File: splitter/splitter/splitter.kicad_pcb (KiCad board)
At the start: 2 copper layers, 52 x 92.4 mm, 41 parts, among them J1 JACKIN, J10 Conn_01x08, J11 Conn_01x08, J2 JACKSEND, J3 JACKRECV, J4 JACKOUT, J5 Jack-DC, J6 JACKSEND2, J8 JACKRECV2, SW1 SW_MODE, SW2 SW_BYPASS, U1 TL074, U2 TLE2426xLP

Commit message: updated generated outputs and docs
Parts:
- C1, C2: value 22n -> 6.8n
- C3, C4: value .1u -> 1u
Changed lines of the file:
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@@
       (effects (font (size 1 1) (thickness 0.15)))
     )
-    (fp_text value "22n" (at 2.5 0) (layer "F.SilkS")
+    (fp_text value "6.8n" (at 2.5 0) (layer "F.SilkS")
       (effects (font (size 1 1) (thickness 0.15)))
     )
@@
       (effects (font (size 1 1) (thickness 0.15)))
     )
-    (fp_text value "22n" (at 2.5 0) (layer "F.SilkS")
+    (fp_text value "6.8n" (at 2.5 0) (layer "F.SilkS")
       (effects (font (size 1 1) (thickness 0.15)))
     )
@@
       (effects (font (size 1 1) (thickness 0.15)))
     )
-    (fp_text user "${REFERENCE}" (at 3.81 7.62) (layer "F.Fab")
+    (fp_text user "${REFERENCE}" (at 3.81 7.62) (layer "F.Fab") hide
       (effects (font (size 1 1) (thickness 0.15)))
     )
@@
       (effects (font (size 1 1) (thickness 0.15)))
     )
-    (fp_text value ".1u" (at 1.25 3.75 90) (layer "F.Fab")
+    (fp_text value "1u" (at 1.25 3.75 90) (layer "F.Fab")
       (effects (font (size 1 1) (thickness 0.15)))
     )
@@
       (effects (font (size 1 1) (thickness 0.15)))
     )
-    (fp_text value ".1u" (at 1.25 3.75 90) (layer "F.Fab")
+    (fp_text value "1u" (at 1.25 3.75 90) (layer "F.Fab")
       (effects (font (size 1 1) (thickness 0.15)))
     )
@@
     (effects (font (size 1 1) (thickness 0.15)) (justify left))
   )
-  (gr_text "JLCJLCJLCJLC" (at 5.08 61.452 90) (layer "F.SilkS")
+  (gr_text "JLCJLCJLCJLC" (at 55 61.8 90) (layer "F.SilkS")
     (effects (font (size 1 1) (thickness 0.15)))
   )

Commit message: rev e
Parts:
- removed the R4 at (27.5, 60.5)
- removed the R5 at (32.0, 60.5)
- C2: renamed from C1; footprint kicad-official/Capacitor_THT.pretty:C_Disc_D4.3mm_W1.9mm_P5.00mm -> kicad-official/Capacitor_THT.pretty:C_Rect_L7.0mm_W2.5mm_P5.00mm
- C3: renamed from C2; footprint kicad-official/Capacitor_THT.pretty:C_Disc_D4.3mm_W1.9mm_P5.00mm -> kicad-official/Capacitor_THT.pretty:C_Rect_L7.0mm_W2.5mm_P5.00mm
- moved R6 8.81 mm to (50.5, 34.8), turned to 180 degrees
- moved R4 7.62 mm to (40.9, 45.2), turned to 90 degrees
- moved C1 6.68 mm to (27.2, 56.1), turned to 0 degrees
- moved C5 5.00 mm to (37.3, 43.6), turned to 90 degrees
- moved C8 4.54 mm to (32.2, 59.7), turned to 180 degrees
- moved C7 3.94 mm to (49.0, 30.8)
- moved C6 0.13 mm to (19.5, 37.4)
- renumbered C5 to C1, C4 to C10, C7 to C4, C6 to C5, C8 to C6, C9 to C7, C10 to C8, C3 to C9, J6 to J3, J3 to J4, J8 to J5, J4 to J6, J5 to J7, J10 to J8, J11 to J9, JP2 to JP1, JP1 to JP2, R9 to R10, R6 to R4, R7 to R5, R8 to R6, R10 to R7, R11 to R8, R12 to R9, SW2 to SW1, SW1 to SW2
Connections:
- C1 pad 1: Net-(C5-Pad1) -> Net-(C1-Pad1)
- C4 pad 1: /SEND_2 -> Net-(C4-Pad1)
- C4 pad 2: Net-(C7-Pad2) -> /HIGH
- C5 pad 1: Net-(C6-Pad1) -> Net-(C5-Pad1)
- C5 pad 2: /SEND_1 -> /LOW
- R3 pad 2: /HIGH -> Net-(C4-Pad1)
- R4 pad 1: /LOW -> Net-(C5-Pad1)
- RV1 pad 5: /HIGH -> Net-(C4-Pad1)
- RV1 pad 6: /HIGH -> Net-(C4-Pad1)
- SW2 pad 2: /HALF_IN -> /IN
- SW2 pad 3: Net-(C6-Pad1) -> /SEND_1
- SW2 pad 6: /HALF_IN -> /IN
- SW2 pad 7: Net-(C7-Pad2) -> /SEND_2
- U1 pad 1: /HIGH -> Net-(C4-Pad1)
- U1 pad 12: /HALF_IN -> Net-(C1-Pad1)
- U1 pad 14: /LOW -> Net-(C5-Pad1)
- U1 pad 2: /HIGH -> Net-(C4-Pad1)
- U1 pad 5: Net-(C5-Pad1) -> Net-(C1-Pad1)
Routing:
- net /HALF_IN: track 54.9 -> 0.00 mm
- net Net-(C4-Pad1): track 0.00 -> 51.1 mm, vias 0 -> 1
- net /IN: track 31.7 -> 71.0 mm, vias 0 -> 1
- net /SEND_1: track 30.7 -> 55.8 mm
- net /HIGH: track 44.5 -> 20.9 mm, vias 1 -> 0
- net Net-(C1-Pad1): track 0.00 -> 22.3 mm
- net Net-(C6-Pad1): track 22.2 -> 0.00 mm, vias 1 -> 0
- net GND: track 82.2 -> 63.9 mm
- net Net-(C7-Pad2): track 12.4 -> 0.00 mm
- net /SEND_2: track 82.8 -> 73.4 mm
- net Net-(C5-Pad1): track 22.3 -> 15.6 mm
- net Net-(C7-Pad1): track 4.52 -> 9.59 mm
- net /LOW: track 31.3 -> 27.4 mm
- net /RECV_2: track 94.8 -> 91.2 mm
- net Net-(C8-Pad1): track 29.5 -> 32.2 mm
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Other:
- board size 52 x 92.4 mm -> 52 x 92.5 mm
- board text added: "REV.E TONE SPLITTER 2023-09-28"
- board text removed: "REV.D TONE SPLITTER 2023-08-31"

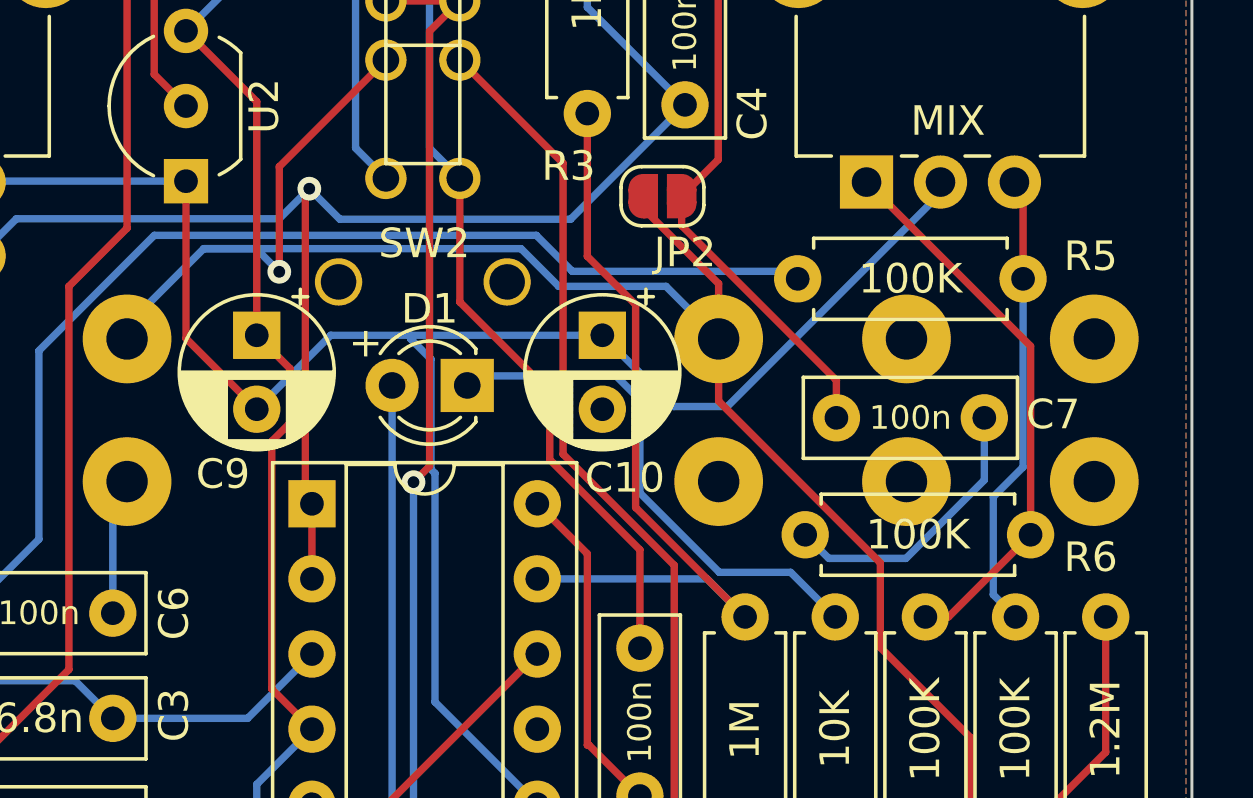
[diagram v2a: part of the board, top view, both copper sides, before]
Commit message: update capacitor footprints
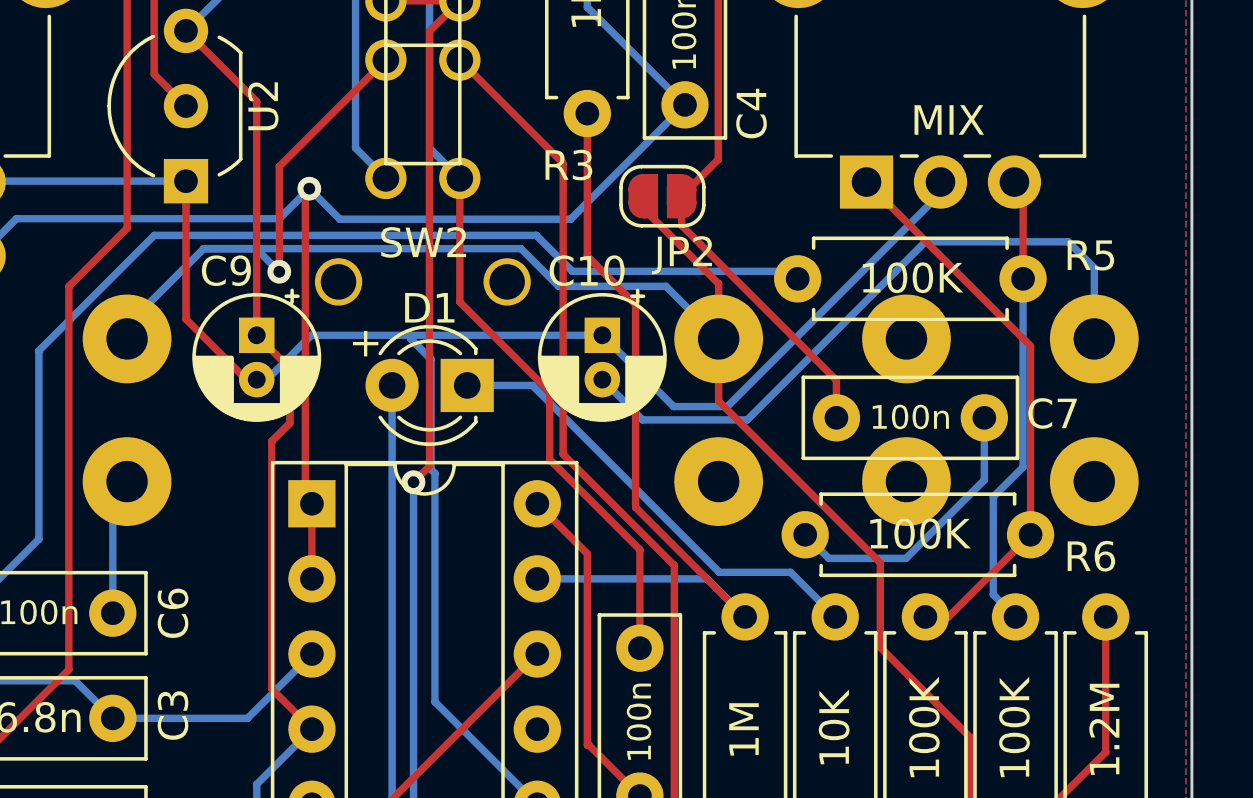
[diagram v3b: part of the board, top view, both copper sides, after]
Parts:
- C10, C9: footprint kicad-official/Capacitor_THT.pretty:CP_Radial_D5.0mm_P2.50mm -> kicad-official/Capacitor_THT.pretty:CP_Radial_D4.0mm_P1.50mm
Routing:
- net GNDD: track 10.1 -> 32.5 mm
- net GND: track 63.9 -> 62.0 mm
- net Net-(D1-Pad1): track 17.3 -> 15.7 mm

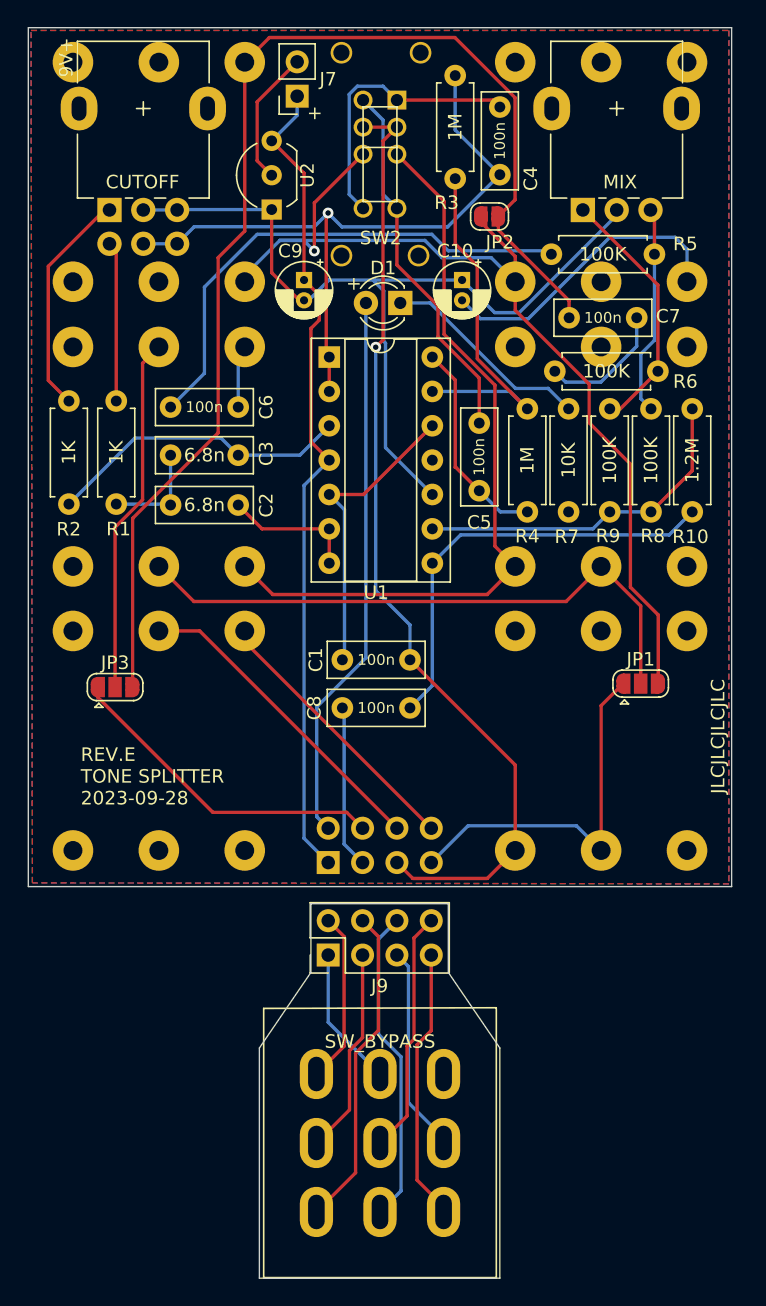
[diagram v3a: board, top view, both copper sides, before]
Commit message: switch to IPC cables for switch
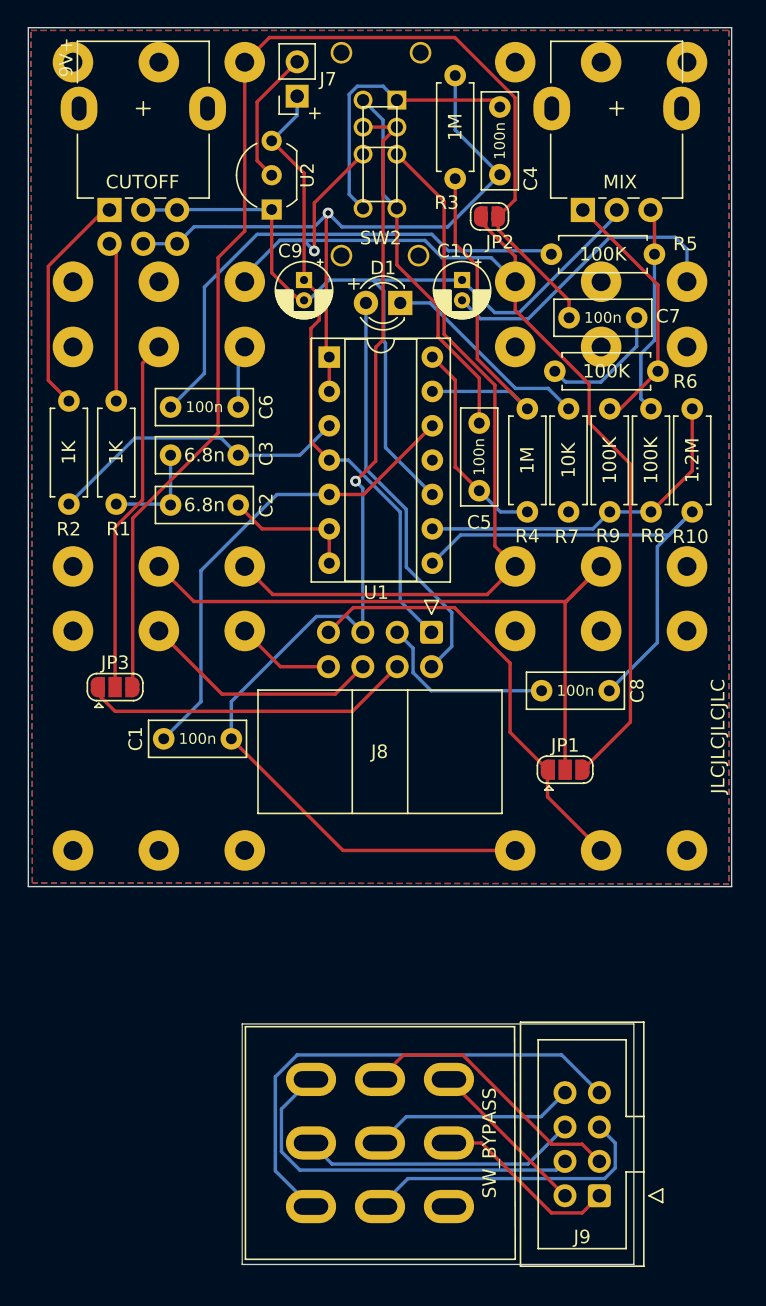
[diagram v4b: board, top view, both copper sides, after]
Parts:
- J8: footprint kicad-official/Connector_PinSocket_2.54mm.pretty:PinSocket_2x04_P2.54mm_Vertical -> kicad-official/Connector_IDC.pretty:IDC-Header_2x04_P2.54mm_Horizontal; moved to F.Cu
- J9: footprint kicad-official/Connector_PinHeader_2.54mm.pretty:PinHeader_2x04_P2.54mm_Vertical -> kicad-official/Connector_IDC.pretty:IDC-Header_2x04_P2.54mm_Vertical
- moved J9 26.8 mm to (46.2, 95.8), turned to 180 degrees
- moved J8 18.7 mm to (33.8, 54.1)
- moved C8 14.8 mm to (47.0, 58.4)
- moved C1 14.4 mm to (14.0, 62.0)
- moved JP1 8.47 mm to (43.7, 64.3)
- turned SW1 to -90 degrees
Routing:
- net /INR_B: track 19.3 -> 36.5 mm
- net +9V: track 61.2 -> 46.7 mm
- net Net-(C1-Pad1): track 22.3 -> 35.1 mm
- net /OUTT: track 19.5 -> 7.28 mm
- net /LED: track 40.7 -> 30.1 mm
- net /IN: track 71.0 -> 81.3 mm
- net /IN_B: track 14.2 -> 22.1 mm
- net /SEND_2: track 73.4 -> 80.4 mm
- net Net-(J2-PadR): track 44.7 -> 51.0 mm
- net /OUTR: track 23.6 -> 17.9 mm
- net /INR: track 27.4 -> 32.5 mm
- net /OUT_B: track 15.3 -> 20.3 mm
- net Net-(C8-Pad1): track 32.2 -> 36.6 mm
- net /RECVR_B: track 23.9 -> 28.0 mm
- net /9V_B: track 10.4 -> 13.8 mm
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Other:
- board size 52 x 92.5 mm -> 52 x 91.4 mm

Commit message: update input buffer
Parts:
- added R11: 1M, Resistor_THT:R_Axial_DIN0207_L6.3mm_D2.5mm_P7.62mm_Horizontal, F.Cu at (11.5, 58.0)
- added R12: 1M, Resistor_THT:R_Axial_DIN0207_L6.3mm_D2.5mm_P7.62mm_Horizontal, F.Cu at (7.00, 58.0)
- C1, C4, C5, C6, C7, C8: value 100n -> 10u; footprint kicad-official/Capacitor_THT.pretty:C_Rect_L7.0mm_W2.5mm_P5.00mm -> Capacitor_SMD:C_0805_2012Metric
- C10, C9: footprint kicad-official/Capacitor_THT.pretty:CP_Radial_D4.0mm_P1.50mm -> Capacitor_SMD:C_0805_2012Metric
- C2, C3: footprint kicad-official/Capacitor_THT.pretty:C_Rect_L7.0mm_W2.5mm_P5.00mm -> Capacitor_THT:C_Rect_L7.0mm_W2.5mm_P5.00mm
- D1: footprint kicad-official/LED_THT.pretty:LED_D3.0mm -> LED_THT:LED_D3.0mm
- J1, J2, J3, J4, J5, J6: footprint kicad-legacy/kicad-footprints/Connector_Audio.pretty:Jack_6.35mm_Neutrik_NMJ6HFD2_Horizontal -> Connector_Audio:Jack_6.35mm_Neutrik_NMJ6HFD2_Horizontal
- R1, R10, R2, R3, R4, R5, R6, R7, R8, R9: footprint kicad-official/Resistor_THT.pretty:R_Axial_DIN0207_L6.3mm_D2.5mm_P7.62mm_Horizontal -> Resistor_THT:R_Axial_DIN0207_L6.3mm_D2.5mm_P7.62mm_Horizontal
- RV1: value CUTOFF -> A1M_DUAL_CUTOFF; footprint kicad-official/Potentiometer_THT.pretty:Potentiometer_Alpha_RD902F-40-00D_Dual_Vertical -> Potentiometer_THT:Potentiometer_Alpha_RD902F-40-00D_Dual_Vertical
- RV2: value MIX -> B10K_MIX; footprint kicad-official/Potentiometer_THT.pretty:Potentiometer_Alpha_RD901F-40-00D_Single_Vertical -> Potentiometer_THT:Potentiometer_Alpha_RD901F-40-00D_Single_Vertical
- moved JP3 6.29 mm to (16.7, 58.0)
- moved C1 4.22 mm to (16.9, 65.0)
- moved C4 1.77 mm to (38.8, 18.5), turned to -90 degrees
- moved C6 1.55 mm to (21.0, 37.0), turned to -90 degrees
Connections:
- C2 pad 2: Net-(C2-Pad2) -> Net-(U1D-+)
- U1 pad 12: Net-(C1-Pad1) -> Net-(U1D-+)
- U1 pad 5: Net-(C1-Pad1) -> GND
- U1 pad 6: Net-(C2-Pad2) -> Net-(U1B--)
- U1 pad 7: Net-(C2-Pad2) -> Net-(U1D-+)
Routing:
- net Net-(U1D-+): track 0.00 -> 46.6 mm, vias 0 -> 1
- net Net-(U1B--): track 0.00 -> 36.5 mm, vias 0 -> 1
- net Net-(C1-Pad1): track 35.1 -> 4.76 mm
- net Net-(U1D--): track 26.8 -> 0.00 mm
- net Net-(C2-Pad2): track 10.0 -> 0.00 mm
- net +9V: track 46.7 -> 37.2 mm
- net /IN: track 81.3 -> 89.8 mm, vias 1 -> 2
- net /RECVR: track 24.6 -> 18.6 mm
- net /RECV_2: track 91.2 -> 96.4 mm
- net Net-(JP3-C): track 26.5 -> 30.2 mm
- net Net-(C6-Pad2): track 37.4 -> 39.8 mm, vias 0 -> 1
- net /HIGH: track 20.9 -> 22.5 mm
- net Net-(U1A--): track 51.1 -> 52.5 mm
- net GNDD: track 32.5 -> 33.6 mm
- net /OUTR: track 17.9 -> 17.1 mm
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
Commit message: redesign board: rev F
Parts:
- C2, C3: footprint Capacitor_THT:C_Rect_L7.0mm_W2.5mm_P5.00mm -> Capacitor_SMD:C_0805_2012Metric
- J7: footprint kicad-official/Connector_PinSocket_2.54mm.pretty:PinSocket_1x02_P2.54mm_Vertical -> Connector_PinSocket_2.54mm:PinSocket_1x02_P2.54mm_Vertical
- J8: footprint kicad-official/Connector_IDC.pretty:IDC-Header_2x04_P2.54mm_Horizontal -> Connector_IDC:IDC-Header_2x04_P2.54mm_Vertical
- J9: footprint kicad-official/Connector_IDC.pretty:IDC-Header_2x04_P2.54mm_Vertical -> Connector_IDC:IDC-Header_2x04_P2.54mm_Vertical
- JP1, JP3: footprint kicad-official/Jumper.pretty:SolderJumper-3_P1.3mm_Open_RoundedPad1.0x1.5mm -> Jumper:SolderJumper-3_P1.3mm_Open_RoundedPad1.0x1.5mm
- JP2: footprint kicad-official/Jumper.pretty:SolderJumper-2_P1.3mm_Open_RoundedPad1.0x1.5mm -> Jumper:SolderJumper-2_P1.3mm_Open_RoundedPad1.0x1.5mm
- R1, R10, R11, R12, R2, R3, R4, R5, R6, R8, R9: footprint Resistor_THT:R_Axial_DIN0207_L6.3mm_D2.5mm_P7.62mm_Horizontal -> Resistor_SMD:R_0805_2012Metric
- R7: value 10K -> 100K; footprint Resistor_THT:R_Axial_DIN0207_L6.3mm_D2.5mm_P7.62mm_Horizontal -> Resistor_SMD:R_0805_2012Metric
- U1: footprint kicad-official/Package_DIP.pretty:DIP-14_W7.62mm_Socket -> Package_DIP:DIP-14_W7.62mm_Socket
- U2: footprint kicad-official/Package_TO_SOT_THT.pretty:TO-92_Inline_Wide -> Package_TO_SOT_THT:TO-92_Inline_Wide
- moved C6 27.3 mm to (47.5, 43.5), turned to 90 degrees
- moved C1 23.5 mm to (17.0, 41.5), turned to 90 degrees
- moved R3 23.4 mm to (39.5, 43.6), turned to -90 degrees
- moved R7 23.1 mm to (24.0, 26.0), turned to 180 degrees
- moved R12 22.3 mm to (22.0, 41.5), turned to 90 degrees
- moved C4 21.4 mm to (45.0, 39.0), turned to 90 degrees
- moved R5 18.8 mm to (50.0, 43.5), turned to 90 degrees
- moved R11 18.3 mm to (19.5, 41.5)
- moved C8 15.0 mm to (45.0, 43.5), turned to -90 degrees
- moved JP3 13.3 mm to (29.7, 55.0)
- moved J8 11.7 mm to (26.2, 63.0), turned to 90 degrees
- moved C7 10.4 mm to (42.5, 39.0), turned to 90 degrees
- moved C3 7.53 mm to (12.0, 41.5), turned to -90 degrees
- moved SW1 6.85 mm to (30.0, 85.0)
- moved J9 6.85 mm to (46.2, 88.9)
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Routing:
- net /RECV_1: track 3.46 -> 51.7 mm, vias 0 -> 1
- net Net-(C6-Pad2): track 39.8 -> 3.27 mm, vias 1 -> 0
- net /RECV_2: track 96.4 -> 65.2 mm, vias 0 -> 3
- net +9V: track 37.2 -> 67.6 mm, vias 0 -> 1
- net Net-(U1B--): track 36.5 -> 10.8 mm, vias 1 -> 0
- net /OUT: track 13.5 -> 33.5 mm, vias 0 -> 1
- net /SEND_2: track 80.4 -> 62.3 mm
- net /HIGH: track 22.5 -> 40.5 mm
- net /LED: track 30.1 -> 12.3 mm
- net Net-(U1D-+): track 46.6 -> 30.9 mm, vias 1 -> 0
- net /INR: track 32.5 -> 18.1 mm
- net Net-(C8-Pad1): track 36.6 -> 22.8 mm
- net /RECVR: track 18.6 -> 5.13 mm
- net /OUTT: track 7.28 -> 20.6 mm
- net GNDD: track 33.6 -> 21.2 mm
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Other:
- board size 52 x 91.4 mm -> 52 x 84.6 mm
- board text added: "REV.F TONE SPLITTER 2025-04-03"
- board text removed: "JLCJLCJLCJLC"
- board text removed: "REV.E TONE SPLITTER 2023-09-28"
- board text removed: "switch shift up 6.85mm"
